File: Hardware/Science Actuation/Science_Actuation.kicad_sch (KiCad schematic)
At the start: 120 parts, among them J2 RJ45_LED_Shielded, Q1 Si4156DY, Q10 Si4156DY, Q11 Si4156DY, Q12 Si4156DY, Q13 Si4156DY, Q14 Si4156DY, Q15 Si4156DY, Q16 Si4156DY, Q2 Si4156DY, Q3 Si4156DY, Q4 Si4156DY, Q5 Si4156DY, Q6 Si4156DY, Q7 Si4156DY, Q8 Si4156DY, Q9 Si4156DY, SW1 SW_Push, SW10 SW_SPDT, SW2 SW_Push, SW3 SW_Push, SW4 SW_Push, SW5 SW_Push, SW6 SW_Push, U10 IRS2308, U11 IRS2308, U12 74LVC2G04, U13 IRS2308, U14 IRS2308, U2 OKI, U2 Teensy4.1_DEV-16771, U3 74LVC2G04, U4 IRS2308, U5 IRS2308, U6 74LVC2G04, U7 IRS2308, U8 IRS2308, U9 74LVC2G04

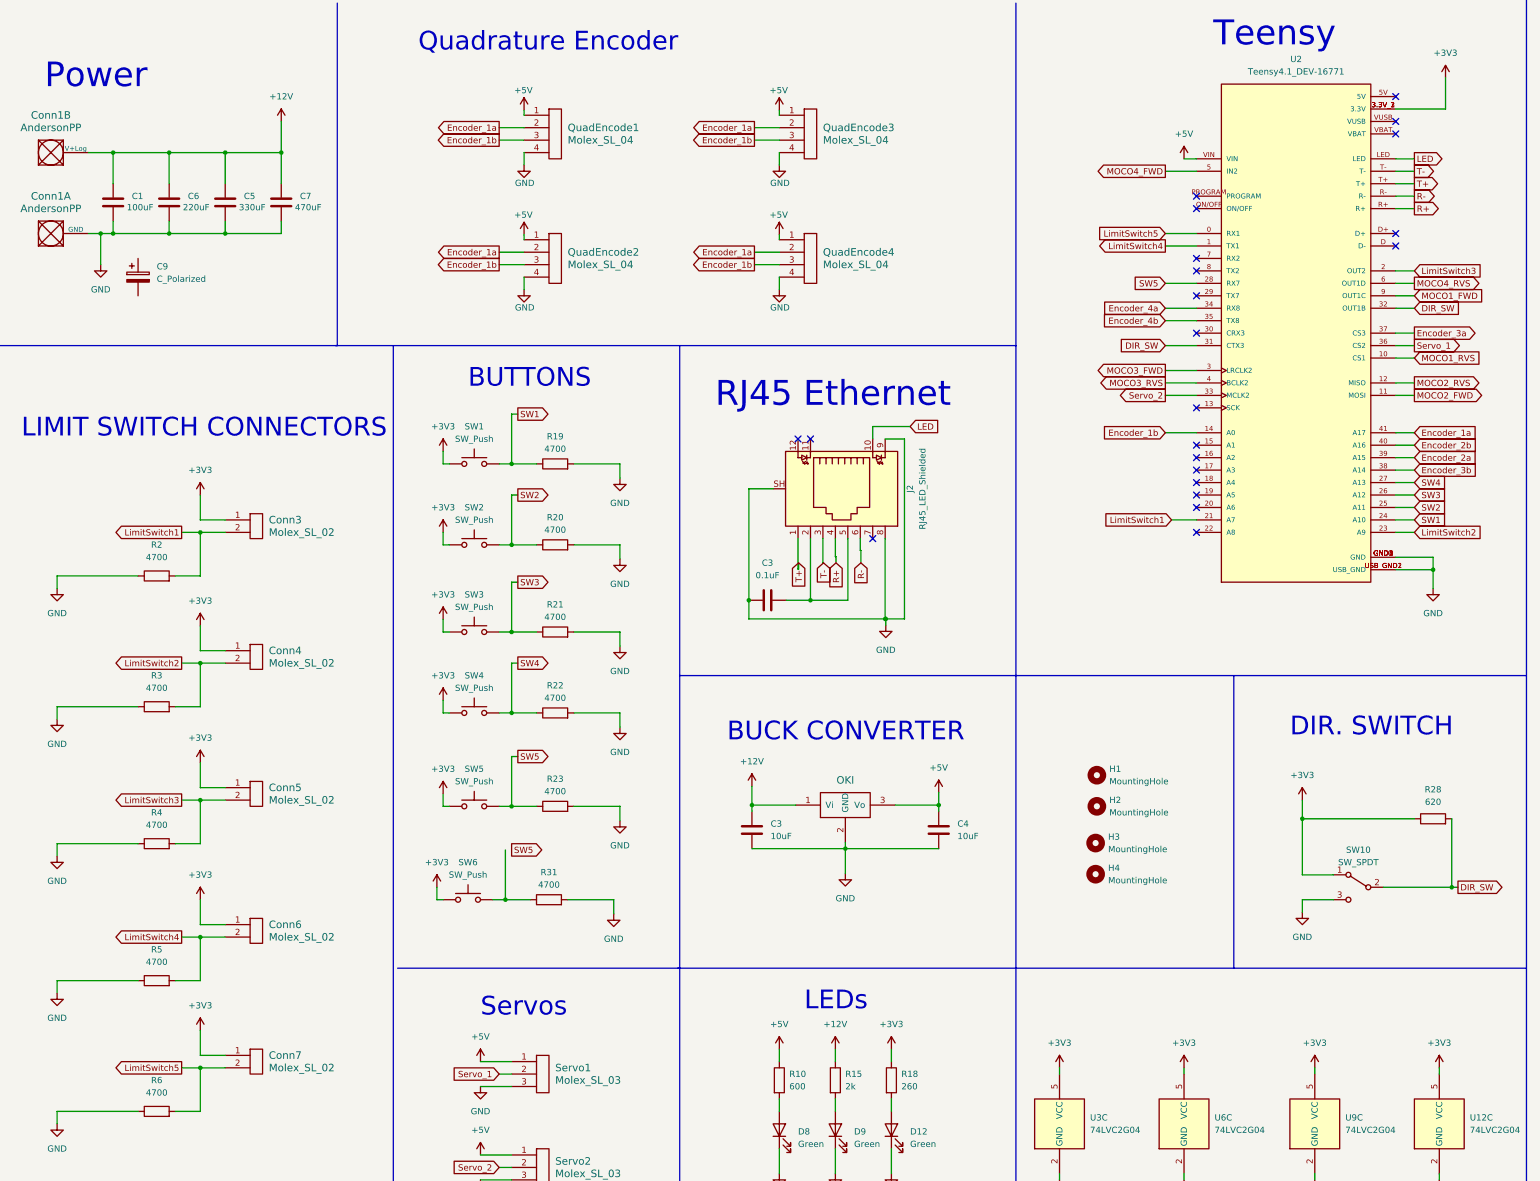
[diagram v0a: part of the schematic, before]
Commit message: Changed Capacitor icons, as well as (hopefully) fixing the LED values to more reasonable amounts. Will still need to change footnotes for Capacitors
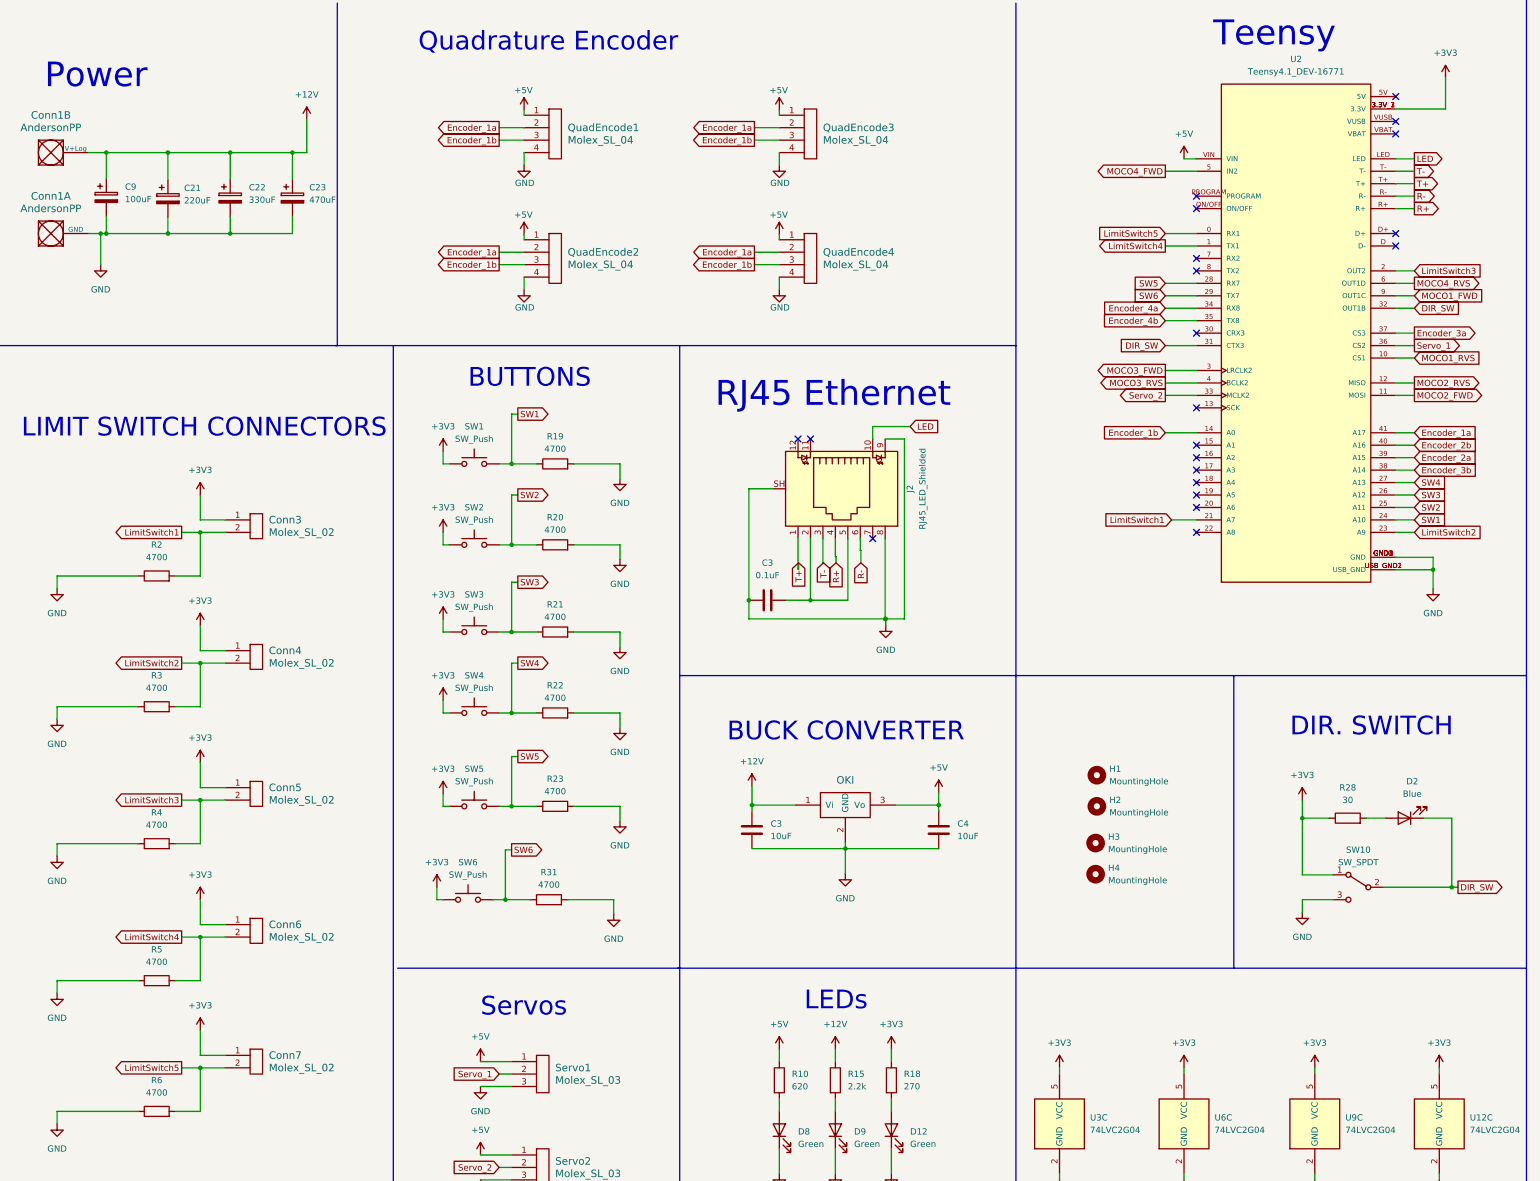
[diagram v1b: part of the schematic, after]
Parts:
- removed C1: 100uF, Capacitor_THT:CP_Radial_D6.3mm_P2.50mm, symbol Device:C
- removed C5: 330uF, Capacitor_THT:CP_Radial_D6.3mm_P2.50mm, symbol Device:C
- removed C6: 220uF, Capacitor_THT:CP_Radial_D6.3mm_P2.50mm, symbol Device:C
- removed C7: 470uF, Capacitor_THT:CP_Radial_D6.3mm_P2.50mm, symbol Device:C
- added C21: 220uF, symbol Device:C_Polarized
- added C22: 330uF, symbol Device:C_Polarized
- added C23: 470uF, symbol Device:C_Polarized
- added D2: Blue, symbol Device:LED
- C9: value C_Polarized -> 100uF
- R10: value 600 -> 620
- R15: value 2k -> 2.2k
- R18: value 260 -> 270
- R28: value 620 -> 30
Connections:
- net +12V: now also C9.1, C21.1, C22.1, C23.1
- net DIR_SW: now also D2.1 (K); no longer R28.2
- net GND: now also C9.2, C21.2, C22.2, C23.2
- net SW6: now reaches R31.1, SW6.2
- net SW6: now also U2.29 (TX7)
- new net: D2.2 (A), R28.2
- no-connect marks 23 -> 22
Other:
- moved on the sheet: C9

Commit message: Finished schematic and first draft of layout
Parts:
- removed C13, C14, C16, C17, C19: 1uF, Capacitor_SMD:C_0603_1608Metric_Pad1.08x0.95mm_HandSolder, symbol Device:C
- removed C15, C18, C20: 10uF, Capacitor_SMD:C_0603_1608Metric_Pad1.08x0.95mm_HandSolder, symbol Device:C
- removed C23: 470uF, symbol Device:C_Polarized
- removed Conn10, Conn8, Conn9: AndersonPP, MRDT_Connectors:Square_Anderson_2_H_Side_By_Side, symbol MRDT_Connectors:AndersonPP
- removed D1, D10, D11, D13, D14, D15, D16, D7: SD0603S04, Diode_SMD:D_0603_1608Metric_Pad1.05x0.95mm_HandSolder, symbol Device:D
- removed Q1, Q10, Q11, Q12, Q13, Q14, Q15, Q16, Q2, Q3, Q4, Q5, Q6, Q7, Q8, Q9: Si4156DY, Package_SO:SOIC-8_3.9x4.9mm_P1.27mm, symbol Transistor_FET:Si4162DY
- removed R1, R29, R30: 100, Resistor_SMD:R_0603_1608Metric_Pad0.98x0.95mm_HandSolder, symbol Device:R
- removed R2, R3, R31: 4700, Resistor_SMD:R_0603_1608Metric_Pad0.98x0.95mm_HandSolder, symbol Device:R
- removed U10, U11, U13, U14, U4, U5, U7, U8: IRS2308, Package_SO:SOIC-8_3.9x4.9mm_P1.27mm, symbol Driver_FET:IRS2308
- removed U12, U3, U6, U9: 74LVC2G04, Package_TO_SOT_SMD:SOT-23-6_Handsoldering, symbol 74xGxx:74LVC2G04
- added C4: 470uF, Capacitor_THT:CP_Radial_D10.0mm_P5.00mm, symbol Device:C_Polarized
- added C9: 100nF, Capacitor_SMD:C_0603_1608Metric_Pad1.08x0.95mm_HandSolder, symbol Device:C
- added Conn17: Molex_SL_02, MRDT_Connectors:MOLEX_SL_02_Vertical, symbol MRDT_Connectors:Molex_SL_02
- added Conn3, Conn4, Conn5: AndersonPP, MRDT_Connectors:Square_Anderson_2_H_Side_By_Side, symbol MRDT_Connectors:AndersonPP
- added R10, R18: 1k, Resistor_SMD:R_0603_1608Metric_Pad0.98x0.95mm_HandSolder, symbol Device:R
- added R15: 10k, Resistor_SMD:R_0603_1608Metric_Pad0.98x0.95mm_HandSolder, symbol Device:R
- added U3, U4, U5, U6: VNH7070AS, Package_SO:SOIC-16_3.9x9.9mm_P1.27mm, symbol MRDT_Devices:VNH7070AS
- C1: renamed from C9; footprint (none) -> Capacitor_THT:CP_Radial_D6.3mm_P2.50mm
- C10, C11, C8: value 1uF -> 100nF
- C12: value 10uF -> 10nF
- C2: renamed from C21; footprint (none) -> Capacitor_THT:CP_Radial_D6.3mm_P2.50mm
- C3: renamed from C22; footprint (none) -> Capacitor_THT:CP_Radial_D8.0mm_P3.50mm
- D4: renamed from D2; footprint (none) -> LED_SMD:LED_0603_1608Metric_Pad1.05x0.95mm_HandSolder
- H1, H2, H3, H4: footprint MRDT_Drill_Holes:4_40_Hole_Corner -> MRDT_Drill_Holes:4_40_Hole
- R11, R12, R13, R16, R17, R24, R25, R7: value 100 -> 1k
- R14, R26, R8: value 100 -> 330
- R19, R22, R23, R4, R5, R6: value 4700 -> 1k
- R2: renamed from R10; value 620 -> 820
- R20: value 4700 -> 330
- R21: value 4700 -> 10k
- R27, R9: value 100 -> 10k
- R28: value 30 -> 220
- R3: renamed from R18; value 270 -> 330
- renumbered C3 to C5, C4 to C6, Conn3 to Conn10, Conn4 to Conn11, Conn5 to Conn12, Conn6 to Conn13, Conn7 to Conn14, Servo1 to Conn15, Servo2 to Conn16, QuadEncode1 to Conn6, QuadEncode2 to Conn7, QuadEncode3 to Conn8, QuadEncode4 to Conn9, D9 to D1, D8 to D2, D12 to D3, R15 to R1, SW10 to SW7
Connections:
- net MOCO1_RVS is gone; now on net M2_IN_B: U2.10 (CS1)
- net MOCO2_RVS is gone; now on net M2_SEL: U2.12 (MISO)
- net MOCO3_RVS is gone; now on net M4_SEL: U2.4 (BCLK2)
- net MOCO4_FWD is gone; now on net M4_PWM: U2.5 (IN2)
- net MOCO4_RVS is gone; now on net M3_IN_B: U2.6 (OUT1D)
- net +12V: now also C10.2, C11.2, C8.2, C4.1, C9.2, U3.12 (VCC), U3.4 (VCC), U3.5 (VCC), U4.12 (VCC), U4.4 (VCC), U4.5 (VCC), U5.12 (VCC), U5.4 (VCC), U5.5 (VCC), U6.12 (VCC), U6.4 (VCC), U6.5 (VCC); no longer C12.1
- net +3V3: no longer Conn10.1, Conn11.1, Conn12.1, Conn13.1, Conn14.1, SW1.1, SW2.1, SW3.1, SW4.1, SW5.1, SW6.1
- net DIR_SW: now also U2.17 (A3); no longer U2.31 (CTX3), U2.32 (OUT1B)
- net GND: now also C10.1, C11.1, C8.1, Conn10.2, Conn11.2, Conn12.2, Conn13.2, Conn14.2, R14.2, R26.2, R8.2, SW1.1, SW2.1, SW3.1, SW4.1, SW5.1, SW6.1, C4.2, C9.1, Conn17.2, U3.1 (GND_A), U3.16 (GND_A), U3.8 (GND_B), U3.9 (GND_B), U4.1 (GND_A), U4.16 (GND_A), U4.8 (GND_B), U4.9 (GND_B), U5.1 (GND_A), U5.16 (GND_A), U5.8 (GND_B), U5.9 (GND_B), U6.1 (GND_A), U6.16 (GND_A), U6.8 (GND_B), U6.9 (GND_B); no longer C3.1, J2.SH, R19.2, R21.2, R22.2, R23.2, R4.1, R5.1, R6.1
- net Servo_1: now also U2.18 (A4); no longer U2.36 (CS2)
- net Servo_2: now also U2.19 (A5); no longer U2.33 (MCLK2)
- net M4_SEL: now reaches R25.1
- net at R25.2: now also U6.14 (SEL)
- net M2_PWM: now reaches R12.1
- net M2_PWM: now also U2.25 (A11)
- net at R12.2: now also U4.11 (PWM)
- net M2_IN_B: now reaches R11.1
- net at R11.2: now also U4.6 (IN_B)
- net M1_SEL: now reaches R7.1
- net M1_SEL: now also U2.28 (RX7)
- net at R14.1: now also R15.1, U4.13 (CS)
- net M3_IN_B: now reaches R17.1
- net at R17.2: now also U5.6 (IN_B)
- net at R13.2: now also U4.14 (SEL)
- net at R8.1: now also R9.1, U3.13 (CS)
- net M3_IN_A: now reaches R16.1
- net M3_IN_A: now also U2.7 (RX2)
- net at R16.2: now also U5.3 (IN_A)
- net at R7.2: now also U3.14 (SEL)
- net M2_SEL: now reaches R13.1
- net CS: now reaches R9.2
- net CS: now also C12.1, R21.2, R27.2, U2.24 (A10), R15.2
- net at R27.1: now also R26.1, U6.13 (CS)
- net at R24.2: now also U6.11 (PWM)
- net ENC_4B: now reaches U2.13 (SCK)
- net ENC_4B: now also Conn9.3
- net ENC_3A: now reaches U2.15 (A1)
- net ENC_3A: now also Conn8.2
- net ENC_3B: now reaches U2.16 (A2)
- net ENC_3B: now also Conn8.3
- net SW_3: now reaches U2.20 (A6)
- net SW_3: now also SW3.2
- net SW_5: now reaches U2.22 (A8)
- net SW_5: now also SW5.2
- net M3_SEL: now reaches U2.8 (TX2)
- net M3_SEL: now also R19.1
- net M4_PWM: now reaches R24.1
- removed net Encoder_1a: Conn6.2, Conn7.2, Conn8.2, Conn9.2, U2.41 (A17)
- removed net Encoder_1b: Conn6.3, Conn7.3, Conn8.3, Conn9.3, U2.14 (A0)
- net Encoder_2a renamed ENC_2A
- net ENC_2A: now also Conn7.2
- net Encoder_2b renamed ENC_1A
- net ENC_1A: now also Conn6.2
- net Encoder_3a renamed LIM_1
- net LIM_1: now also Conn10.1
- net Encoder_3b renamed ENC_2B
- net ENC_2B: now also Conn7.3
- net Encoder_4a renamed LIM_3
- net LIM_3: now also Conn12.1
- net Encoder_4b renamed LIM_4
- net LIM_4: now also Conn13.1
- net LimitSwitch1 renamed SW_4
- net SW_4: now also SW4.2; no longer Conn10.2
- net LimitSwitch2 renamed SW_6
- net SW_6: now also SW6.2; no longer Conn11.2
- removed net LimitSwitch3: Conn12.2, R4.2, U2.2 (OUT2)
- removed net LimitSwitch4: Conn13.2, R5.2, U2.1 (TX1)
- removed net LimitSwitch5: Conn14.2, R6.2, U2.0 (RX1)
- removed net M+: C11.2, C8.2, Conn2.1 (GND)
- net M- renamed M1+
- net M1+: now also U3.15 (OUT_A), U3.2 (OUT_A); no longer C10.2
- net MOCO1_FWD renamed M3_PWM
- net M3_PWM: now also R18.1
- net MOCO2_FWD renamed M2_IN_A
- net M2_IN_A: now also R10.1
- net MOCO3_FWD renamed M4_IN_A
- net M4_IN_A: now also R22.1
- removed net SW1: R19.1, SW1.2, U2.24 (A10)
- removed net SW2: R20.1, SW2.2, U2.25 (A11)
- removed net SW3: R21.1, SW3.2, U2.26 (A12)
- removed net SW4: R22.1, SW4.2, U2.27 (A13)
- removed net SW5: R23.1, SW5.2, U2.28 (RX7)
- net SW6 renamed M1_PWM
- net M1_PWM: now also R6.1; no longer SW6.2
- new net: R19.2, U5.14 (SEL)
- new net: C3.1, J2.SH
- new net: R10.2, U4.3 (IN_A)
- new net: R18.2, U5.11 (PWM)
- new net: R20.1, R21.1, U5.13 (CS)
- new net: R22.2, U6.3 (IN_A)
- new net: R23.2, U6.6 (IN_B)
- new net: R5.2, U3.6 (IN_B)
- new net: R4.2, U3.3 (IN_A)
- new net: R6.2, U3.11 (PWM)
- new net ENC_1B: Conn6.3, U2.41 (A17)
- new net ENC_4A: Conn9.2, U2.14 (A0)
- new net LIM_2: Conn11.1, U2.36 (CS2)
- new net LIM_5: Conn14.1, U2.33 (MCLK2)
- new net LIM_6: Conn17.1, U2.32 (OUT1B)
- new net M1-: Conn2.1 (GND), U3.10 (OUT_B), U3.7 (OUT_B)
- new net M1_IN_A: R4.1, U2.27 (A13)
- new net M1_IN_B: R5.1, U2.26 (A12)
- new net M2+: Conn3.2 (V+Log), U4.15 (OUT_A), U4.2 (OUT_A)
- new net M2-: Conn3.1 (GND), U4.10 (OUT_B), U4.7 (OUT_B)
- new net M3+: Conn4.2 (V+Log), U5.15 (OUT_A), U5.2 (OUT_A)
- new net M3-: Conn4.1 (GND), U5.10 (OUT_B), U5.7 (OUT_B)
- new net M4+: Conn5.2 (V+Log), U6.15 (OUT_A), U6.2 (OUT_A)
- new net M4-: Conn5.1 (GND), U6.10 (OUT_B), U6.7 (OUT_B)
- new net M4_IN_B: R23.1, U2.2 (OUT2)
- new net SW_1: SW1.2, U2.1 (TX1)
- new net SW_2: SW2.2, U2.0 (RX1)
- no-connect marks 22 -> 10
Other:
- note added: "DIR SWITCH"
- note added: "LIMIT SWITCHES"
- note added: "Motor Controllers"
- note added: "Quadrature Encoders"
- note removed: "BUCK CONVERTER"
- note removed: "DIR. SWITCH"
- note removed: "H-Bridge"
- note removed: "LEDs"
- note removed: "LIMIT SWITCH CONNECTORS"
- note removed: "MOCO Breakout"
- note removed: "Quadrature Encoder"
- moved on the sheet: C1, C2, C3, C5, C6, Conn10, Conn11, Conn12, Conn13, Conn14, Conn15, Conn16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

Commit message: Finish layout
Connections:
- no-connect marks 10 -> 12
